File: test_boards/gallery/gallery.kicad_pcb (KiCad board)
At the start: 2 copper layers, 33 parts

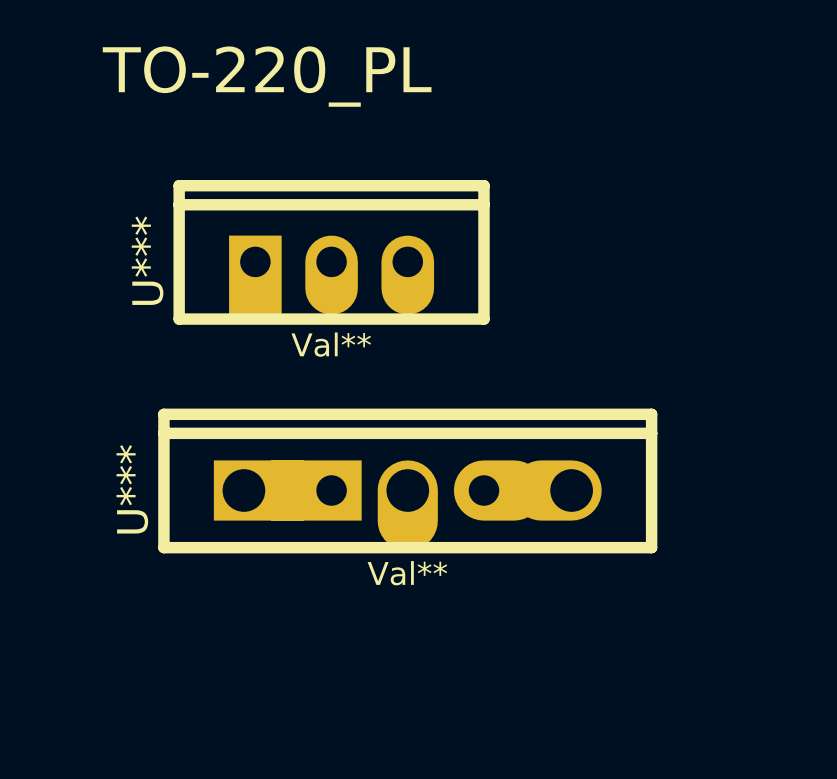
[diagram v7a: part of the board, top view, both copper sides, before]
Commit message: adding 7812 regulator.  updating line thickness of to-220 footprints.
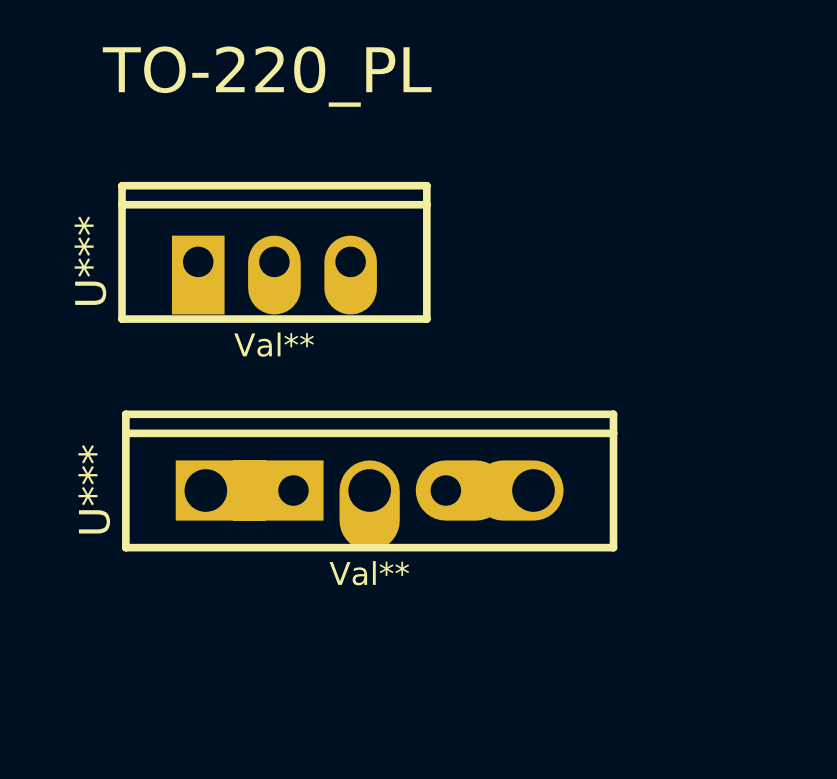
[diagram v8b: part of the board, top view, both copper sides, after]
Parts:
- moved Val** 1.91 mm to (21.0, 58.4)
- moved Val** 1.27 mm to (24.1, 66.0)
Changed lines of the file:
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@@
     (pcb_text_width 0.3)
     (pcb_text_size 1.5 1.5)
-    (mod_edge_width 0.3048)
+    (mod_edge_width 0.254)
     (mod_text_size 1 1)
     (mod_text_width 0.15)
@@
     )
   )
-  (module TO-220_V_069B (layer F.Cu)
-    (at 22.86 58.42)
-    (descr "TO-220, vertical, 0.04\" holes, 0.069\" pads")
-    (tags "TR TO220")
-    (fp_text reference Val** (at 2.54 2.794) (layer F.SilkS)
-      (effects (font (size 0.762 0.762) (thickness 0.1524)))
-    )
-    (fp_text value U*** (at -3.556 0 90) (layer F.SilkS)
-      (effects (font (size 1.016 1.016) (thickness 0.2032)))
-    )
-    (fp_line (start -2.54 -1.905) (end -2.54 -2.54) (layer F.SilkS) (width 0.381))
-    (fp_line (start -2.54 -2.54) (end 7.62 -2.54) (layer F.SilkS) (width 0.381))
-    (fp_line (start 7.62 -2.54) (end 7.62 -1.905) (layer F.SilkS) (width 0.381))
-    (fp_line (start -2.54 1.905) (end -2.54 -1.905) (layer F.SilkS) (width 0.381))
-    (fp_line (start -2.54 -1.905) (end 7.62 -1.905) (layer F.SilkS) (width 0.381))
-    (fp_line (start 7.62 -1.905) (end 7.62 1.905) (layer F.SilkS) (width 0.381))
-    (fp_line (start 7.62 1.905) (end -2.54 1.905) (layer F.SilkS) (width 0.381))
-    (pad 1 thru_hole rect (at 0 0 90) (size 2.6289 1.7526) (drill 1.016 (offset -0.43815 0))
-      (layers *.Cu *.Mask F.SilkS)
-    )
-    (pad 2 thru_hole oval (at 2.54 0 90) (size 2.6289 1.7526) (drill 1.016 (offset -0.43815 0))
-      (layers *.Cu *.Mask F.SilkS)
-    )
-    (pad 3 thru_hole oval (at 5.08 0 90) (size 2.6289 1.7526) (drill 1.016 (offset -0.43815 0))
-      (layers *.Cu *.Mask F.SilkS)
-    )
-  )
-  (module TO-220_TO-218_TO-247_V_079B (layer F.Cu)
-    (at 25.4 66.04)
-    (descr "TO-220, TO-218, and TO-247 vertical, 079B pads")
-    (tags "TR TO220")
-    (fp_text reference Val** (at 2.54 2.794) (layer F.SilkS)
-      (effects (font (size 0.762 0.762) (thickness 0.1524)))
-    )
-    (fp_text value U*** (at -6.604 0 90) (layer F.SilkS)
-      (effects (font (size 1.016 1.016) (thickness 0.2032)))
-    )
-    (fp_line (start -5.588 -1.905) (end -5.588 -2.54) (layer F.SilkS) (width 0.381))
-    (fp_line (start -5.588 -2.54) (end 10.668 -2.54) (layer F.SilkS) (width 0.381))
-    (fp_line (start 10.668 -2.54) (end 10.668 -1.905) (layer F.SilkS) (width 0.381))
-    (fp_line (start -5.588 1.905) (end -5.588 -1.905) (layer F.SilkS) (width 0.381))
-    (fp_line (start -5.588 -1.905) (end 10.668 -1.905) (layer F.SilkS) (width 0.381))
-    (fp_line (start 10.668 -1.905) (end 10.668 1.905) (layer F.SilkS) (width 0.381))
-    (fp_line (start 10.668 1.905) (end -5.588 1.905) (layer F.SilkS) (width 0.381))
-    (pad 1 thru_hole rect (at 0 0 90) (size 2.0066 3.0099) (drill 1.016 (offset 0 -0.50165))
-      (layers *.Cu *.Mask F.SilkS)
-    )
-    (pad 2 thru_hole oval (at 2.54 0 90) (size 3.0099 2.0066) (drill 1.4224 (offset -0.50165 0))
-      (layers *.Cu *.Mask F.SilkS)
-    )
-    (pad 3 thru_hole oval (at 5.08 0 90) (size 2.0066 3.0099) (drill 1.016 (offset 0 0.50165))
-      (layers *.Cu *.Mask F.SilkS)
-    )
-    (pad 1 thru_hole rect (at -2.921 0 90) (size 2.0066 3.0099) (drill 1.4224 (offset 0 0.50165))
-      (layers *.Cu *.Mask F.SilkS)
-    )
-    (pad 3 thru_hole oval (at 8.001 0 90) (size 2.0066 3.0099) (drill 1.4224 (offset 0 -0.50165))
-      (layers *.Cu *.Mask F.SilkS)
-    )
-  )
   (module TO-92_Q (layer F.Cu)
     (at 33.02 124.46)
@@
       (layers *.Cu *.Mask F.SilkS)
     )
+  )
+  (module TO-220_V_069B (layer F.Cu)
+    (at 20.955 58.42)
+    (descr "TO-220, vertical, 0.04\" holes, 0.069\" pads")
+    (tags "TR TO220")
+    (fp_text reference Val** (at 2.54 2.794) (layer F.SilkS)
+      (effects (font (size 0.762 0.762) (thickness 0.1524)))
+    )
+    (fp_text value U*** (at -3.556 0 90) (layer F.SilkS)
+      (effects (font (size 1.016 1.016) (thickness 0.2032)))
+    )
+    (fp_line (start -2.54 -1.905) (end -2.54 -2.54) (layer F.SilkS) (width 0.254))
+    (fp_line (start -2.54 -2.54) (end 7.62 -2.54) (layer F.SilkS) (width 0.254))
+    (fp_line (start 7.62 -2.54) (end 7.62 -1.905) (layer F.SilkS) (width 0.254))
+    (fp_line (start -2.54 1.905) (end -2.54 -1.905) (layer F.SilkS) (width 0.254))
+    (fp_line (start -2.54 -1.905) (end 7.62 -1.905) (layer F.SilkS) (width 0.254))
+    (fp_line (start 7.62 -1.905) (end 7.62 1.905) (layer F.SilkS) (width 0.254))
+    (fp_line (start 7.62 1.905) (end -2.54 1.905) (layer F.SilkS) (width 0.254))
+    (pad 1 thru_hole rect (at 0 0 90) (size 2.6289 1.7526) (drill 1.016 (offset -0.43815 0))
+      (layers *.Cu *.Mask F.SilkS)
+    )
+    (pad 2 thru_hole oval (at 2.54 0 90) (size 2.6289 1.7526) (drill 1.016 (offset -0.43815 0))
+      (layers *.Cu *.Mask F.SilkS)
+    )
+    (pad 3 thru_hole oval (at 5.08 0 90) (size 2.6289 1.7526) (drill 1.016 (offset -0.43815 0))
+      (layers *.Cu *.Mask F.SilkS)
+    )
+  )
+  (module TO-220_TO-218_TO-247_V_079B (layer F.Cu)
+    (at 24.13 66.04)
+    (descr "TO-220, TO-218, and TO-247 vertical, 079B pads")
+    (tags "TR TO220")
+    (fp_text reference Val** (at 2.54 2.794) (layer F.SilkS)
+      (effects (font (size 0.762 0.762) (thickness 0.1524)))
+    )
+    (fp_text value U*** (at -6.604 0 90) (layer F.SilkS)
+      (effects (font (size 1.016 1.016) (thickness 0.2032)))
+    )
+    (fp_line (start -5.588 -1.905) (end -5.588 -2.54) (layer F.SilkS) (width 0.254))
+    (fp_line (start -5.588 -2.54) (end 10.668 -2.54) (layer F.SilkS) (width 0.254))
+    (fp_line (start 10.668 -2.54) (end 10.668 -1.905) (layer F.SilkS) (width 0.254))
+    (fp_line (start -5.588 1.905) (end -5.588 -1.905) (layer F.SilkS) (width 0.254))
+    (fp_line (start -5.588 -1.905) (end 10.668 -1.905) (layer F.SilkS) (width 0.254))
+    (fp_line (start 10.668 -1.905) (end 10.668 1.905) (layer F.SilkS) (width 0.254))
+    (fp_line (start 10.668 1.905) (end -5.588 1.905) (layer F.SilkS) (width 0.254))
+    (pad 1 thru_hole rect (at 0 0 90) (size 2.0066 3.0099) (drill 1.016 (offset 0 -0.50165))
+      (layers *.Cu *.Mask F.SilkS)
+    )
+    (pad 2 thru_hole oval (at 2.54 0 90) (size 3.0099 2.0066) (drill 1.4224 (offset -0.50165 0))
+      (layers *.Cu *.Mask F.SilkS)
+    )
+    (pad 3 thru_hole oval (at 5.08 0 90) (size 2.0066 3.0099) (drill 1.016 (offset 0 0.50165))
+      (layers *.Cu *.Mask F.SilkS)
+    )
+    (pad 1 thru_hole rect (at -2.921 0 90) (size 2.0066 3.0099) (drill 1.4224 (offset 0 0.50165))
+      (layers *.Cu *.Mask F.SilkS)
+    )
+    (pad 3 thru_hole oval (at 8.001 0 90) (size 2.0066 3.0099) (drill 1.4224 (offset 0 -0.50165))
+      (layers *.Cu *.Mask F.SilkS)
+    )
